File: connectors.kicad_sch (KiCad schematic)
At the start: 8 parts, among them J1 Conn_01x04_Socket, J2 Conn_01x04_Socket, U3 TPS7A20xxxDBV, U4 TPS7A20xxxDBV

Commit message: chore: fix the naming of connectors sheet file name
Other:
- title: (none) -> ${SHEETNAME}
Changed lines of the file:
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@@
 	(generator_version "9.0")
 	(paper "A4")
+	(title_block
+		(title "${SHEETNAME}")
+	)
 	(junction
 		(at 64.77 57.15)
@@
 		)
 		(instances
-			(project ""
+			(project "wall_moisture-hardware"
 				(path "/dedd74c5-8e82-403a-8a1b-f763d3ee00bb/6d9e78ef-2aac-40ff-a2f1-475c572a17ad"
 					(reference "#PWR04")
@@
 		)
 		(instances
-			(project ""
+			(project "wall_moisture-hardware"
 				(path "/dedd74c5-8e82-403a-8a1b-f763d3ee00bb/6d9e78ef-2aac-40ff-a2f1-475c572a17ad"
 					(reference "U3")
@@
 		)
 		(instances
-			(project ""
+			(project "wall_moisture-hardware"
 				(path "/dedd74c5-8e82-403a-8a1b-f763d3ee00bb/6d9e78ef-2aac-40ff-a2f1-475c572a17ad"
 					(reference "#PWR01")
@@
 		)
 		(instances
-			(project ""
+			(project "wall_moisture-hardware"
 				(path "/dedd74c5-8e82-403a-8a1b-f763d3ee00bb/6d9e78ef-2aac-40ff-a2f1-475c572a17ad"
 					(reference "U4")
@@
 		)
 		(instances
-			(project ""
+			(project "wall_moisture-hardware"
 				(path "/dedd74c5-8e82-403a-8a1b-f763d3ee00bb/6d9e78ef-2aac-40ff-a2f1-475c572a17ad"
 					(reference "#FLG02")
@@
 		)
 		(instances
-			(project ""
+			(project "wall_moisture-hardware"
 				(path "/dedd74c5-8e82-403a-8a1b-f763d3ee00bb/6d9e78ef-2aac-40ff-a2f1-475c572a17ad"
 					(reference "C3")

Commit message: chore: update project to use local footprint and symbols
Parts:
- C3, C4, C5, C6: footprint Capacitor_SMD:C_0603_1608Metric -> footprints:C_0603_1608Metric; symbol Device:C -> symbols:C
- J1, J2: footprint Connector_JST:JST_PH_S4B-PH-SM4-TB_1x04-1MP_P2.00mm_Horizontal -> footprints:JST_PH_S4B-PH-SM4-TB_1x04-1MP_P2.00mm_Horizontal; symbol Connector:Conn_01x04_Socket -> symbols:Conn_01x04_Socket
- U3, U4: footprint Package_TO_SOT_SMD:SOT-23-5 -> footprints:SOT-23-5; symbol el_ce-linear_regulator:TPS7A20xxxDBV -> symbols:TPS7A20xxxDBV
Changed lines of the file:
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@@
 	)
 	(symbol
-		(lib_id "Device:C")
+		(lib_id "symbols:C")
 		(at 147.32 36.83 0)
 		(unit 1)
@@
 			)
 		)
-		(property "Footprint" "Capacitor_SMD:C_0603_1608Metric"
+		(property "Footprint" "footprints:C_0603_1608Metric"
 			(at 148.2852 40.64 0)
 			(effects
@@
 	)
 	(symbol
-		(lib_id "Device:C")
+		(lib_id "symbols:C")
 		(at 102.87 38.1 0)
 		(unit 1)
@@
 			)
 		)
-		(property "Footprint" "Capacitor_SMD:C_0603_1608Metric"
+		(property "Footprint" "footprints:C_0603_1608Metric"
 			(at 103.8352 41.91 0)
 			(effects
@@
 	)
 	(symbol
-		(lib_id "power:GND")
+		(lib_id "symbols:GND")
 		(at 52.07 67.31 0)
 		(unit 1)
@@
 	)
 	(symbol
-		(lib_id "Device:C")
+		(lib_id "symbols:C")
 		(at 125.73 38.1 0)
 		(unit 1)
@@
 			)
 		)
-		(property "Footprint" "Capacitor_SMD:C_0603_1608Metric"
+		(property "Footprint" "footprints:C_0603_1608Metric"
 			(at 126.6952 41.91 0)
 			(effects
@@
 	)
 	(symbol
-		(lib_id "el_ce-linear_regulator:TPS7A20xxxDBV")
+		(lib_id "symbols:TPS7A20xxxDBV")
 		(at 92.71 34.29 0)
 		(unit 1)
@@
 			)
 		)
-		(property "Footprint" "Package_TO_SOT_SMD:SOT-23-5"
+		(property "Footprint" "footprints:SOT-23-5"
 			(at 92.71 25.4 0)
 			(effects
@@
 			)
 		)
-		(property "Datasheet" "https://www.ti.com/lit/ds/symlink/tps7a20.pdf"
+		(property "Datasheet" ""
 			(at 92.71 21.59 0)
 			(effects
@@
 			)
 		)
-		(property "Description" "300 mA Low Dropout Voltage Regulator, Fixed Output, 1.6..6.0Vin, Low-Noise (7μV RMS), 6.5μA IQ LDO, SOT-23-5"
+		(property "Description" ""
 			(at 92.202 44.704 0)
 			(effects
@@
 	)
 	(symbol
-		(lib_id "Connector:Conn_01x04_Socket")
+		(lib_id "symbols:Conn_01x04_Socket")
 		(at 43.18 62.23 180)
 		(unit 1)
@@
 			)
 		)
-		(property "Footprint" "Connector_JST:JST_PH_S4B-PH-SM4-TB_1x04-1MP_P2.00mm_Horizontal"
+		(property "Footprint" "footprints:JST_PH_S4B-PH-SM4-TB_1x04-1MP_P2.00mm_Horizontal"
 			(at 43.18 62.23 0)
 			(effects
@@
 	)
 	(symbol
-		(lib_id "power:+5V")
+		(lib_id "symbols:+5V")
 		(at 54.61 50.8 0)
 		(unit 1)
@@
 	)
 	(symbol
-		(lib_id "power:+5V")
+		(lib_id "symbols:+5V")
 		(at 77.47 27.94 0)
 		(unit 1)
@@
 	)
 	(symbol
-		(lib_id "power:+5V")
+		(lib_id "symbols:+5V")
 		(at 121.92 26.67 0)
 		(unit 1)
@@
 	)
 	(symbol
-		(lib_id "el_ce-linear_regulator:TPS7A20xxxDBV")
+		(lib_id "symbols:TPS7A20xxxDBV")
 		(at 137.16 34.29 0)
 		(unit 1)
@@
 			)
 		)
-		(property "Footprint" "Package_TO_SOT_SMD:SOT-23-5"
+		(property "Footprint" "footprints:SOT-23-5"
 			(at 137.16 25.4 0)
 			(effects
@@
 			)
 		)
-		(property "Datasheet" "https://www.ti.com/lit/ds/symlink/tps7a20.pdf"
+		(property "Datasheet" ""
 			(at 137.16 21.59 0)
 			(effects
@@
 			)
 		)
-		(property "Description" "300 mA Low Dropout Voltage Regulator, Fixed Output, 1.6..6.0Vin, Low-Noise (7μV RMS), 6.5μA IQ LDO, SOT-23-5"
+		(property "Description" ""
 			(at 136.652 44.704 0)
 			(effects
@@
 	)
 	(symbol
-		(lib_id "power:PWR_FLAG")
+		(lib_id "symbols:PWR_FLAG")
 		(at 54.61 53.34 270)
 		(unit 1)
@@
 	)
 	(symbol
-		(lib_id "power:GND")
+		(lib_id "symbols:GND")
 		(at 137.16 45.72 0)
 		(unit 1)
@@
 	)
 	(symbol
-		(lib_id "power:PWR_FLAG")
+		(lib_id "symbols:PWR_FLAG")
 		(at 52.07 102.87 90)
 		(unit 1)
@@
 	)
 	(symbol
-		(lib_id "Connector:Conn_01x04_Socket")
+		(lib_id "symbols:Conn_01x04_Socket")
 		(at 43.18 97.79 180)
 		(unit 1)
@@
 			)
 		)
-		(property "Footprint" "Connector_JST:JST_PH_S4B-PH-SM4-TB_1x04-1MP_P2.00mm_Horizontal"
+		(property "Footprint" "footprints:JST_PH_S4B-PH-SM4-TB_1x04-1MP_P2.00mm_Horizontal"
 			(at 43.18 97.79 0)
 			(effects
@@
 	)
 	(symbol
-		(lib_id "power:GND")
+		(lib_id "symbols:GND")
 		(at 92.71 45.72 0)
 		(unit 1)
@@
 	)
 	(symbol
-		(lib_id "power:GND")
+		(lib_id "symbols:GND")
 		(at 52.07 104.14 0)
 		(unit 1)
@@
 	)
 	(symbol
-		(lib_id "Device:C")
+		(lib_id "symbols:C")
 		(at 77.47 38.1 0)
 		(unit 1)
@@
 			)
 		)
-		(property "Footprint" "Capacitor_SMD:C_0603_1608Metric"
+		(property "Footprint" "footprints:C_0603_1608Metric"
 			(at 78.4352 41.91 0)
 			(effects

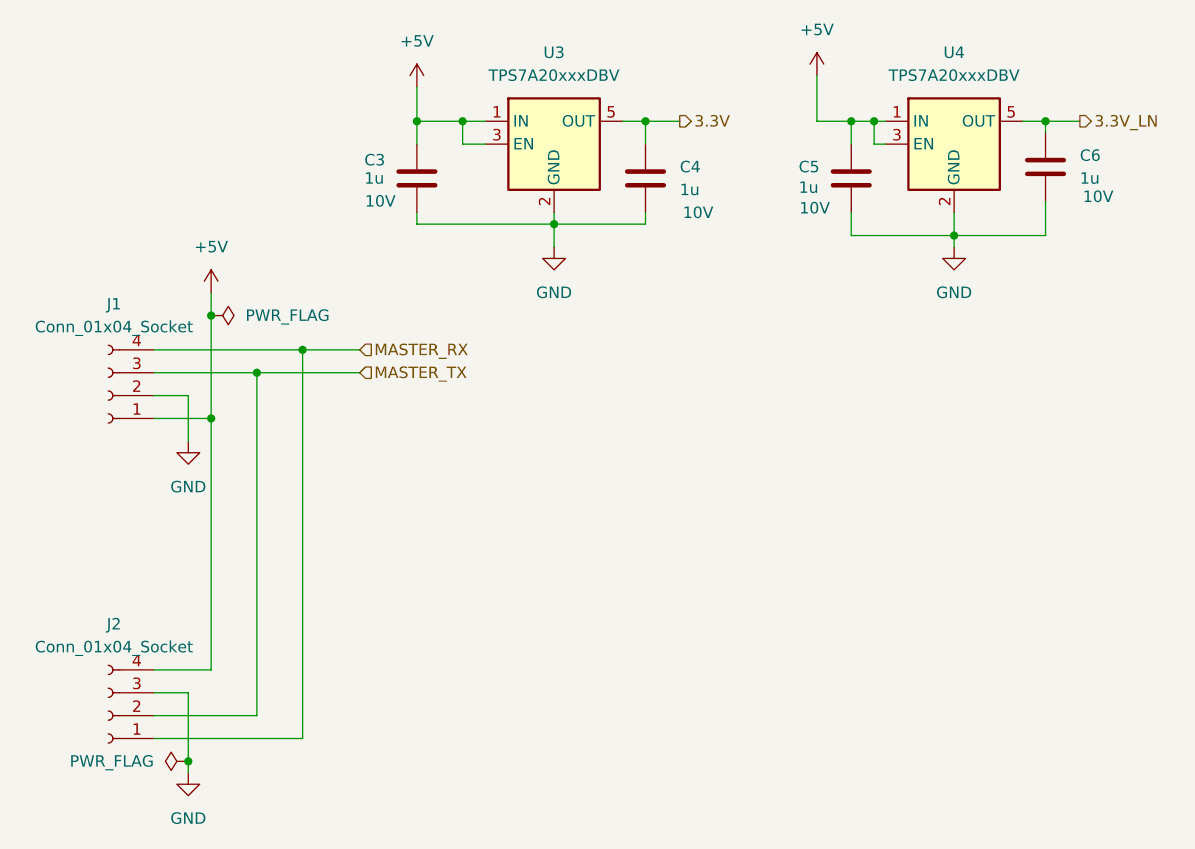
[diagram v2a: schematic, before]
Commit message: design: Assign LSCS and MPN reference to components
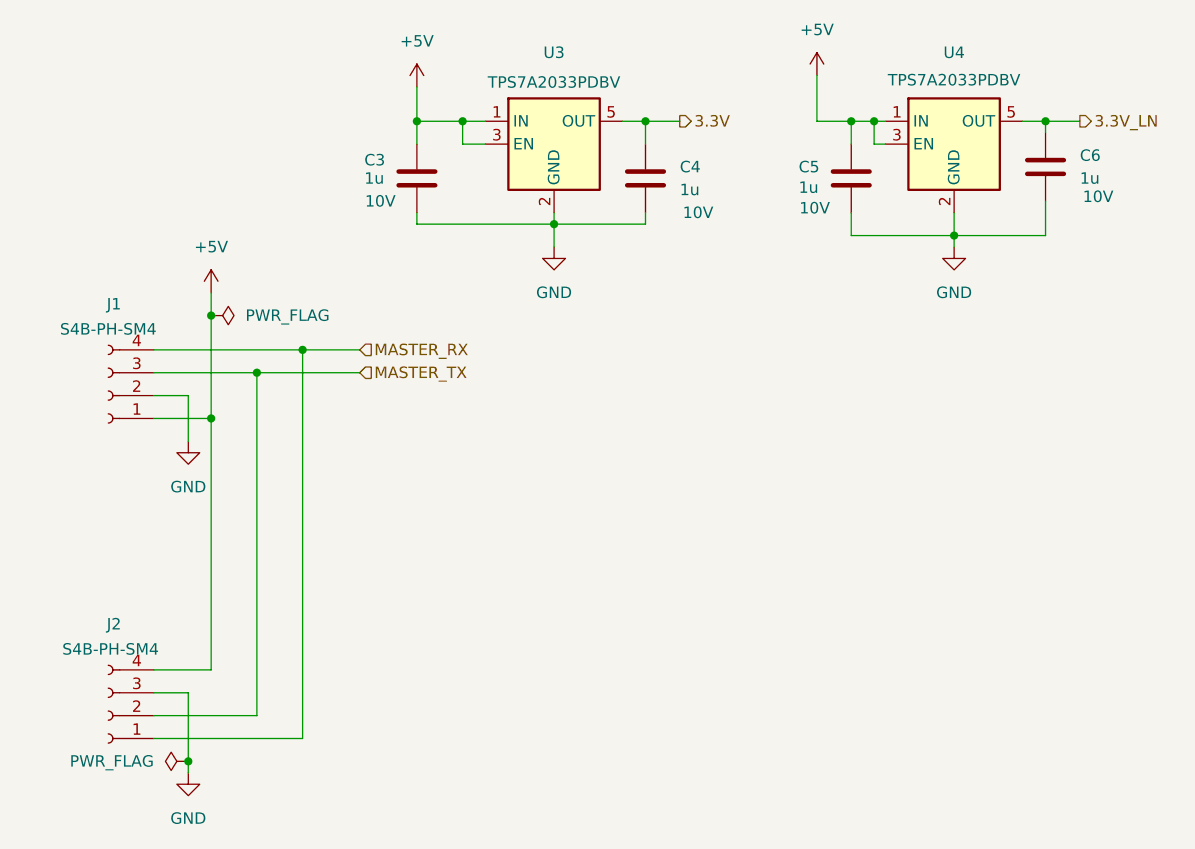
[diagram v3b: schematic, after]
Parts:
- C3, C4, C5, C6: LCSC (none) -> C59782
- J1, J2: value Conn_01x04_Socket -> ~; LCSC (none) -> C265102; MPN (none) -> S4B-PH-SM4
- U3, U4: value TPS7A20xxxDBV -> ~; LCSC (none) -> C2862740; MPN (none) -> TPS7A2033PDBV
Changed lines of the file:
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@@
+			)
+		)
+		(property "LCSC" "C59782"
+			(at 147.32 36.83 0)
+			(effects
+				(font
+					(size 1.27 1.27)
+				)
+				(hide yes)
 			)
 		)
@@
 					(size 1.27 1.27)
 				)
+			)
+		)
+		(property "LCSC" "C59782"
+			(at 102.87 38.1 0)
+			(effects
+				(font
+					(size 1.27 1.27)
+				)
+				(hide yes)
 			)
 		)
@@
 			)
 		)
+		(property "LCSC" "C59782"
+			(at 125.73 38.1 0)
+			(effects
+				(font
+					(size 1.27 1.27)
+				)
+				(hide yes)
+			)
+		)
 		(pin "1"
 		)
@@
 		(on_board yes)
 		(dnp no)
-		(fields_autoplaced yes)
 		(property "Reference" "U3"
 			(at 92.71 24.13 0)
@@
 			)
 		)
-		(property "Value" "TPS7A20xxxDBV"
+		(property "Value" "~"
 			(at 92.71 26.67 0)
 			(effects
@@
 			)
 		)
-		(property "Datasheet" ""
+		(property "Datasheet" "https://www.ti.com/lit/ds/symlink/tps7a20.pdf"
 			(at 92.71 21.59 0)
 			(effects
@@
 			)
 		)
+		(property "LCSC" "C2862740"
+			(at 92.71 34.29 0)
+			(effects
+				(font
+					(size 1.27 1.27)
+				)
+				(hide yes)
+			)
+		)
+		(property "MPN" "TPS7A2033PDBV"
+			(at 92.71 27.432 0)
+			(effects
+				(font
+					(size 1.27 1.27)
+				)
+			)
+		)
 		(pin "1"
 		)
@@
 		(on_board yes)
 		(dnp no)
-		(fields_autoplaced yes)
 		(property "Reference" "J1"
 			(at 43.815 52.07 0)
@@
 			)
 		)
-		(property "Value" "Conn_01x04_Socket"
+		(property "Value" "~"
 			(at 43.815 54.61 0)
 			(effects
@@
 				)
 				(hide yes)
+			)
+		)
+		(property "LCSC" "C265102"
+			(at 43.18 62.23 0)
+			(effects
+				(font
+					(size 1.27 1.27)
+				)
+				(hide yes)
+			)
+		)
+		(property "MPN" "S4B-PH-SM4"
+			(at 43.18 54.864 0)
+			(effects
+				(font
+					(size 1.27 1.27)
+				)
 			)
 		)
@@
 		(on_board yes)
 		(dnp no)
-		(fields_autoplaced yes)
 		(property "Reference" "U4"
 			(at 137.16 24.13 0)
@@
 			)
 		)
-		(property "Value" "TPS7A20xxxDBV"
+		(property "Value" "~"
 			(at 137.16 26.67 0)
 			(effects
@@
 			)
 		)
-		(property "Datasheet" ""
+		(property "Datasheet" "https://www.ti.com/lit/ds/symlink/tps7a20.pdf"
 			(at 137.16 21.59 0)
 			(effects
@@
 				)
 				(hide yes)
+			)
+		)
+		(property "LCSC" "C2862740"
+			(at 137.16 34.29 0)
+			(effects
+				(font
+					(size 1.27 1.27)
+				)
+				(hide yes)
+			)
+		)
+		(property "MPN" "TPS7A2033PDBV"
+			(at 137.16 27.178 0)
+			(effects
+				(font
+					(size 1.27 1.27)
+				)
 			)
 		)
@@
 		(on_board yes)
 		(dnp no)
-		(fields_autoplaced yes)
 		(property "Reference" "J2"
 			(at 43.815 87.63 0)
@@
 			)
 		)
-		(property "Value" "Conn_01x04_Socket"
+		(property "Value" "~"
 			(at 43.815 90.17 0)
 			(effects
@@
 				)
 				(hide yes)
+			)
+		)
+		(property "LCSC" "C265102"
+			(at 43.18 97.79 0)
+			(effects
+				(font
+					(size 1.27 1.27)
+				)
+				(hide yes)
+			)
+		)
+		(property "MPN" "S4B-PH-SM4"
+			(at 43.434 90.424 0)
+			(effects
+				(font
+					(size 1.27 1.27)
+				)
 			)
 		)
@@
 			)
 		)
+		(property "LCSC" "C59782"
+			(at 77.47 38.1 0)
+			(effects
+				(font
+					(size 1.27 1.27)
+				)
+				(hide yes)
+			)
+		)

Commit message: design: Assign the project version and project company from project variable, which are then substituted during the ci
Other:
- company: (none) -> ${COMPANY}
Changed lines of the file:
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@@
 	(title_block
 		(title "${SHEETNAME}")
+		(rev "${VERSION}")
+		(company "${COMPANY}")
 	)
 	(junction

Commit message: bom: Optimize part selection to reduce order price at jlcpcb
- Change references to use basic components instead of 'extended components' when available
- Change button reference to use a basic component
- Change led references to use basic components
- Harmonize some resistors value to limit the number of lines in BoM
- Change transistor references for basic components
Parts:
- C3, C4, C5, C6: LCSC C59782 -> C15849
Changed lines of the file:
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@@
 			)
 		)
-		(property "LCSC" "C59782"
+		(property "LCSC" "C15849"
 			(at 147.32 36.83 0)
 			(effects
@@
 				)
 				(hide yes)
+			)
+		)
+		(property "MPN" ""
+			(at 147.32 36.83 0)
+			(effects
+				(font
+					(size 1.27 1.27)
+				)
 			)
 		)
@@
 			)
 		)
-		(property "LCSC" "C59782"
+		(property "LCSC" "C15849"
 			(at 102.87 38.1 0)
 			(effects
@@
 				)
 				(hide yes)
+			)
+		)
+		(property "MPN" ""
+			(at 102.87 38.1 0)
+			(effects
+				(font
+					(size 1.27 1.27)
+				)
 			)
 		)
@@
 			)
 		)
-		(property "LCSC" "C59782"
+		(property "LCSC" "C15849"
 			(at 125.73 38.1 0)
 			(effects
@@
 				)
 				(hide yes)
+			)
+		)
+		(property "MPN" ""
+			(at 125.73 38.1 0)
+			(effects
+				(font
+					(size 1.27 1.27)
+				)
 			)
 		)
@@
 			)
 		)
-		(property "LCSC" "C59782"
+		(property "LCSC" "C15849"
 			(at 77.47 38.1 0)
 			(effects
@@
 			)
 		)
+		(property "MPN" ""
+			(at 77.47 38.1 0)
+			(effects
+				(font
+					(size 1.27 1.27)
+				)
+			)
+		)
